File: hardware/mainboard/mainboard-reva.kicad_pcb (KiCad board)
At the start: 4 copper layers, 88 x 48 mm, 77 parts, among them J1 USB-C, J2 BATTERY, J3 SM05B-GHS-TB / ENCODER, J4 SM03B-GHS-TB / SNOOZE, J5 Molex 54550-2472 / GDEY037T03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, J6 Molex 54550-0672 / FL21 front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, J7 SPEAKER, J8 SM02B-GHS-TB / WAKE_LED, Q2 AO3400A / WAKE, U1 ESP32-S3-WROOM-1-N8, U2 BQ24074RGTR, U3 TPS62840DLCR, U4 RV-3028-C7, U5 VEML7700, U6 MAX98357AETE+T, U7 USBLC6-2SC6

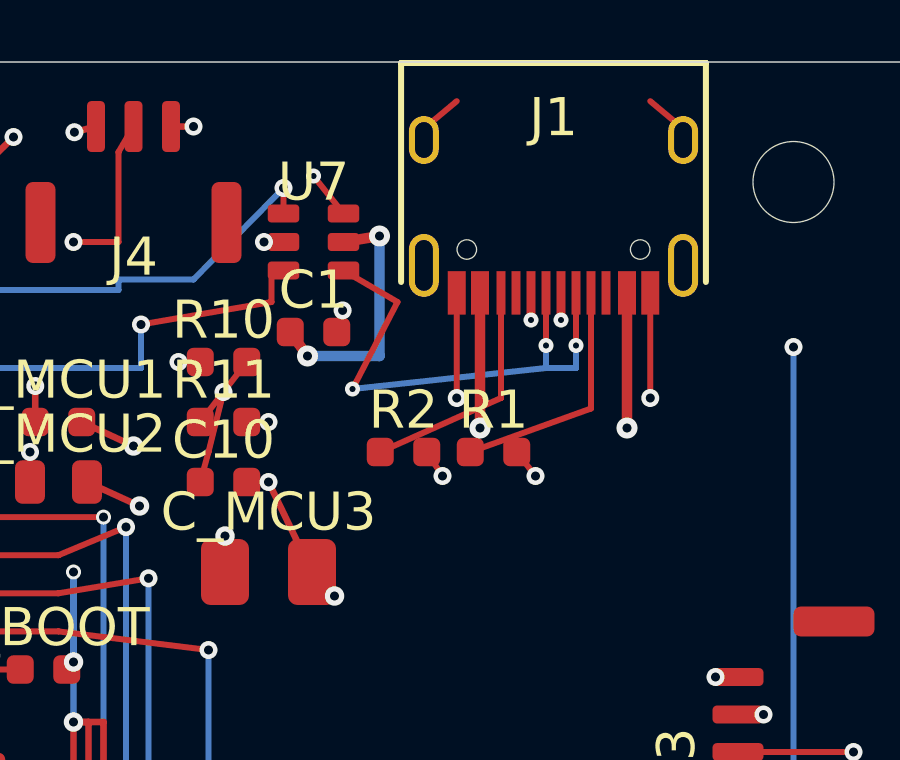
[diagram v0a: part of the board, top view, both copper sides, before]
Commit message: fix(mainboard): finish CC fanout and USB data clearances
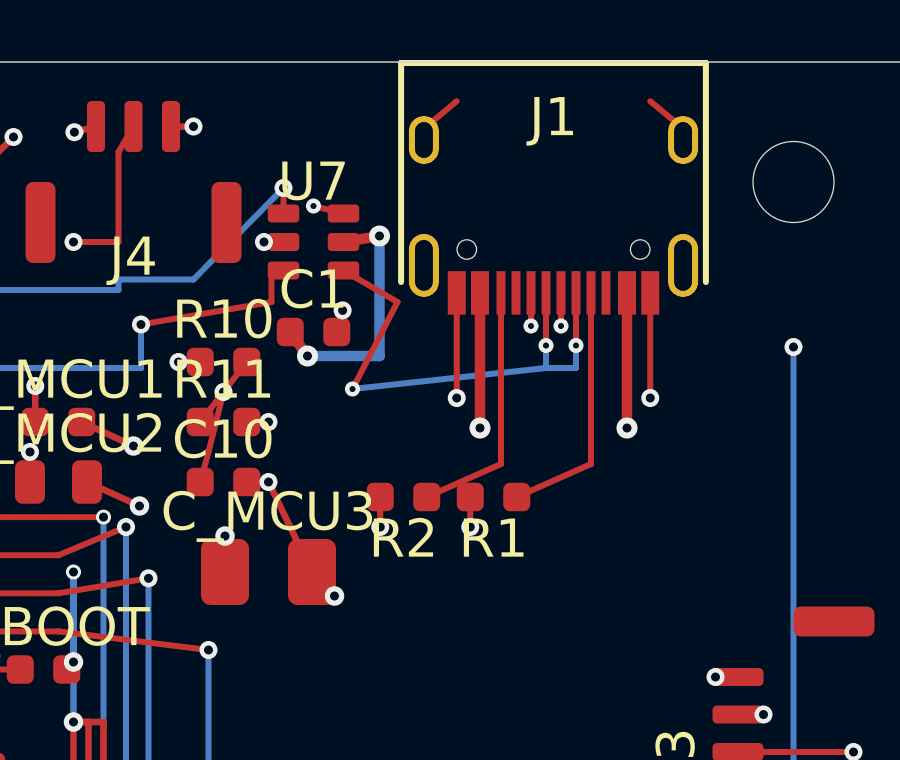
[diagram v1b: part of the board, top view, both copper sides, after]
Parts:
- moved R1 1.50 mm to (74.0, 14.5), turned to 180 degrees
- moved R2 1.50 mm to (71.0, 14.5), turned to 180 degrees
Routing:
- net USB_D+_CONN: track 18.1 -> 16.6 mm
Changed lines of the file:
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@@
     (pad "6" smd roundrect (at 1 -0.95) (size 1.05 0.6) (layers "F.Cu" "F.Paste" "F.Mask") (roundrect_rratio 0.2) (net 59 "USB_D+_CONN"))
   )
-  (footprint "Resistor_SMD:R_0603_1608Metric" (layer "F.Cu") (at 74.0 13.0)
+  (footprint "Resistor_SMD:R_0603_1608Metric" (layer "F.Cu") (at 74.0 14.5 180)
     (property "Reference" "R1" (at 0 -1.4) (layer "F.SilkS"))
     (property "Value" "5.1k CC1" (at 0 1.4) (layer "F.Fab") hide)
@@
     (pad "2" smd roundrect (at 0.775 0) (size 0.9 0.95) (layers "F.Cu" "F.Paste" "F.Mask") (roundrect_rratio 0.25) (net 1 "GND"))
   )
-  (footprint "Resistor_SMD:R_0603_1608Metric" (layer "F.Cu") (at 71.0 13.0)
+  (footprint "Resistor_SMD:R_0603_1608Metric" (layer "F.Cu") (at 71.0 14.5 180)
     (property "Reference" "R2" (at 0 -1.4) (layer "F.SilkS"))
     (property "Value" "5.1k CC2" (at 0 1.4) (layer "F.Fab") hide)
@@
   (segment (start 79.225 7.695) (end 79.225 11.20) (width 0.20) (layer "F.Cu") (net 1))
   (via (at 79.225 11.20) (size 0.60) (drill 0.30) (layers "F.Cu" "B.Cu") (net 1))
-  (segment (start 77.25 7.695) (end 77.25 11.55) (width 0.20) (layer "F.Cu") (net 21))
-  (segment (start 77.25 11.55) (end 73.225 13.00) (width 0.20) (layer "F.Cu") (net 21))
-  (segment (start 71.775 13.00) (end 72.30 13.80) (width 0.20) (layer "F.Cu") (net 1))
-  (via (at 72.30 13.80) (size 0.60) (drill 0.30) (layers "F.Cu" "B.Cu") (net 1))
-  (segment (start 74.25 7.695) (end 74.25 11.20) (width 0.20) (layer "F.Cu") (net 22))
-  (segment (start 74.25 11.20) (end 70.225 13.00) (width 0.20) (layer "F.Cu") (net 22))
-  (segment (start 74.775 13.00) (end 75.40 13.80) (width 0.20) (layer "F.Cu") (net 1))
-  (via (at 75.40 13.80) (size 0.60) (drill 0.30) (layers "F.Cu" "B.Cu") (net 1))
-  (segment (start 75.25 7.695) (end 75.25 8.60) (width 0.20) (layer "F.Cu") (net 59))
-  (via (at 75.25 8.60) (size 0.50) (drill 0.20) (layers "F.Cu" "B.Cu") (net 59))
-  (segment (start 76.25 7.695) (end 76.25 8.60) (width 0.20) (layer "F.Cu") (net 59))
-  (via (at 76.25 8.60) (size 0.50) (drill 0.20) (layers "F.Cu" "B.Cu") (net 59))
-  (segment (start 75.25 8.60) (end 75.25 9.80) (width 0.20) (layer "In1.Cu") (net 59))
-  (segment (start 76.25 8.60) (end 76.25 9.80) (width 0.20) (layer "In1.Cu") (net 59))
+  (segment (start 77.25 7.695) (end 77.25 13.40) (width 0.20) (layer "F.Cu") (net 21))
+  (segment (start 77.25 13.40) (end 74.775 14.50) (width 0.20) (layer "F.Cu") (net 21))
+  (segment (start 73.225 14.50) (end 73.225 15.50) (width 0.20) (layer "F.Cu") (net 1))
+  (via (at 73.225 15.50) (size 0.60) (drill 0.30) (layers "F.Cu" "B.Cu") (net 1))
+  (segment (start 74.25 7.695) (end 74.25 13.40) (width 0.20) (layer "F.Cu") (net 22))
+  (segment (start 74.25 13.40) (end 71.775 14.50) (width 0.20) (layer "F.Cu") (net 22))
+  (segment (start 70.225 14.50) (end 70.225 15.50) (width 0.20) (layer "F.Cu") (net 1))
+  (via (at 70.225 15.50) (size 0.60) (drill 0.30) (layers "F.Cu" "B.Cu") (net 1))
+  (segment (start 75.25 7.695) (end 75.25 8.80) (width 0.20) (layer "F.Cu") (net 59))
+  (via (at 75.25 8.80) (size 0.50) (drill 0.20) (layers "F.Cu" "B.Cu") (net 59))
+  (segment (start 76.25 7.695) (end 76.25 8.80) (width 0.20) (layer "F.Cu") (net 59))
+  (via (at 76.25 8.80) (size 0.50) (drill 0.20) (layers "F.Cu" "B.Cu") (net 59))
+  (segment (start 75.25 8.80) (end 75.25 9.80) (width 0.20) (layer "In1.Cu") (net 59))
+  (segment (start 76.25 8.80) (end 76.25 9.80) (width 0.20) (layer "In1.Cu") (net 59))
   (segment (start 76.25 9.80) (end 75.25 9.80) (width 0.20) (layer "In1.Cu") (net 59))
   (segment (start 75.25 9.80) (end 72.00 10.20) (width 0.20) (layer "In1.Cu") (net 59))
   (segment (start 72.00 10.20) (end 68.00 6.20) (width 0.20) (layer "In1.Cu") (net 59))
-  (segment (start 68.00 6.20) (end 68.00 3.80) (width 0.20) (layer "In1.Cu") (net 59))
-  (via (at 68.00 3.80) (size 0.50) (drill 0.20) (layers "F.Cu" "B.Cu") (net 59))
-  (segment (start 68.00 3.80) (end 69.0 5.05) (width 0.20) (layer "F.Cu") (net 59))
+  (segment (start 68.00 6.20) (end 68.00 4.80) (width 0.20) (layer "In1.Cu") (net 59))
+  (via (at 68.00 4.80) (size 0.50) (drill 0.20) (layers "F.Cu" "B.Cu") (net 59))
+  (segment (start 68.00 4.80) (end 69.0 5.05) (width 0.20) (layer "F.Cu") (net 59))
   (segment (start 75.75 7.695) (end 75.75 9.45) (width 0.20) (layer "F.Cu") (net 60))
   (via (at 75.75 9.45) (size 0.50) (drill 0.20) (layers "F.Cu" "B.Cu") (net 60))

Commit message: fix(mainboard): clear final USB CC and differential breakout conflicts
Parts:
- moved R1 6.00 mm to (80.0, 14.5)
- moved R2 1.00 mm to (72.0, 14.5)
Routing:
- net GND: track 109.5 -> 112.5 mm
- net USB_D+_CONN: track 16.6 -> 17.9 mm
- net USB_CC1: track 8.41 -> 9.40 mm
- net USB_CC2: track 8.41 -> 7.55 mm
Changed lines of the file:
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@@
     (pad "6" smd roundrect (at 1 -0.95) (size 1.05 0.6) (layers "F.Cu" "F.Paste" "F.Mask") (roundrect_rratio 0.2) (net 59 "USB_D+_CONN"))
   )
-  (footprint "Resistor_SMD:R_0603_1608Metric" (layer "F.Cu") (at 74.0 14.5 180)
+  (footprint "Resistor_SMD:R_0603_1608Metric" (layer "F.Cu") (at 80.0 14.5 180)
     (property "Reference" "R1" (at 0 -1.4) (layer "F.SilkS"))
     (property "Value" "5.1k CC1" (at 0 1.4) (layer "F.Fab") hide)
@@
     (pad "2" smd roundrect (at 0.775 0) (size 0.9 0.95) (layers "F.Cu" "F.Paste" "F.Mask") (roundrect_rratio 0.25) (net 1 "GND"))
   )
-  (footprint "Resistor_SMD:R_0603_1608Metric" (layer "F.Cu") (at 71.0 14.5 180)
+  (footprint "Resistor_SMD:R_0603_1608Metric" (layer "F.Cu") (at 72.0 14.5 180)
     (property "Reference" "R2" (at 0 -1.4) (layer "F.SilkS"))
     (property "Value" "5.1k CC2" (at 0 1.4) (layer "F.Fab") hide)
@@
   (via (at 79.225 11.20) (size 0.60) (drill 0.30) (layers "F.Cu" "B.Cu") (net 1))
   (segment (start 77.25 7.695) (end 77.25 13.40) (width 0.20) (layer "F.Cu") (net 21))
-  (segment (start 77.25 13.40) (end 74.775 14.50) (width 0.20) (layer "F.Cu") (net 21))
-  (segment (start 73.225 14.50) (end 73.225 15.50) (width 0.20) (layer "F.Cu") (net 1))
-  (via (at 73.225 15.50) (size 0.60) (drill 0.30) (layers "F.Cu" "B.Cu") (net 1))
+  (segment (start 77.25 13.40) (end 80.775 14.50) (width 0.20) (layer "F.Cu") (net 21))
+  (segment (start 79.225 14.50) (end 79.225 17.00) (width 0.20) (layer "F.Cu") (net 1))
+  (via (at 79.225 17.00) (size 0.60) (drill 0.30) (layers "F.Cu" "B.Cu") (net 1))
   (segment (start 74.25 7.695) (end 74.25 13.40) (width 0.20) (layer "F.Cu") (net 22))
-  (segment (start 74.25 13.40) (end 71.775 14.50) (width 0.20) (layer "F.Cu") (net 22))
-  (segment (start 70.225 14.50) (end 70.225 15.50) (width 0.20) (layer "F.Cu") (net 1))
-  (via (at 70.225 15.50) (size 0.60) (drill 0.30) (layers "F.Cu" "B.Cu") (net 1))
+  (segment (start 74.25 13.40) (end 72.775 14.50) (width 0.20) (layer "F.Cu") (net 22))
+  (segment (start 71.225 14.50) (end 71.225 17.00) (width 0.20) (layer "F.Cu") (net 1))
+  (via (at 71.225 17.00) (size 0.60) (drill 0.30) (layers "F.Cu" "B.Cu") (net 1))
   (segment (start 75.25 7.695) (end 75.25 8.80) (width 0.20) (layer "F.Cu") (net 59))
   (via (at 75.25 8.80) (size 0.50) (drill 0.20) (layers "F.Cu" "B.Cu") (net 59))
   (segment (start 76.25 7.695) (end 76.25 8.80) (width 0.20) (layer "F.Cu") (net 59))
   (via (at 76.25 8.80) (size 0.50) (drill 0.20) (layers "F.Cu" "B.Cu") (net 59))
-  (segment (start 75.25 8.80) (end 75.25 9.80) (width 0.20) (layer "In1.Cu") (net 59))
-  (segment (start 76.25 8.80) (end 76.25 9.80) (width 0.20) (layer "In1.Cu") (net 59))
-  (segment (start 76.25 9.80) (end 75.25 9.80) (width 0.20) (layer "In1.Cu") (net 59))
-  (segment (start 75.25 9.80) (end 72.00 10.20) (width 0.20) (layer "In1.Cu") (net 59))
-  (segment (start 72.00 10.20) (end 68.00 6.20) (width 0.20) (layer "In1.Cu") (net 59))
+  (segment (start 75.25 8.80) (end 75.25 10.30) (width 0.20) (layer "In1.Cu") (net 59))
+  (segment (start 76.25 8.80) (end 76.25 10.30) (width 0.20) (layer "In1.Cu") (net 59))
+  (segment (start 76.25 10.30) (end 75.25 10.30) (width 0.20) (layer "In1.Cu") (net 59))
+  (segment (start 75.25 10.30) (end 72.00 10.70) (width 0.20) (layer "In1.Cu") (net 59))
+  (segment (start 72.00 10.70) (end 68.00 6.20) (width 0.20) (layer "In1.Cu") (net 59))
   (segment (start 68.00 6.20) (end 68.00 4.80) (width 0.20) (layer "In1.Cu") (net 59))
   (via (at 68.00 4.80) (size 0.50) (drill 0.20) (layers "F.Cu" "B.Cu") (net 59))

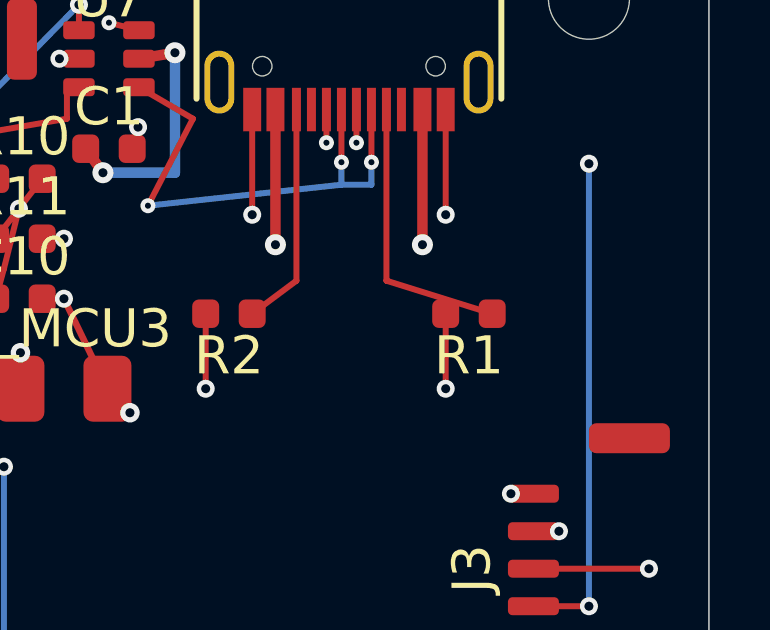
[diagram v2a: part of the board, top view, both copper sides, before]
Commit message: fix(mainboard): orient CC1 pulldown for clean fanout
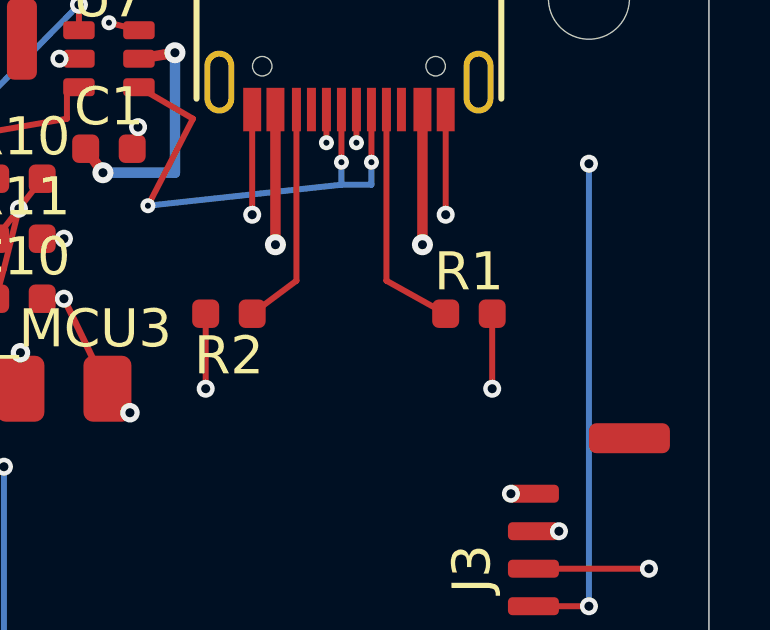
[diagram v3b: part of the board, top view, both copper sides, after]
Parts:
- turned R1 to 0 degrees
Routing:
- net USB_CC1: track 9.40 -> 7.97 mm
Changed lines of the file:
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@@
     (pad "6" smd roundrect (at 1 -0.95) (size 1.05 0.6) (layers "F.Cu" "F.Paste" "F.Mask") (roundrect_rratio 0.2) (net 59 "USB_D+_CONN"))
   )
-  (footprint "Resistor_SMD:R_0603_1608Metric" (layer "F.Cu") (at 80.0 14.5 180)
+  (footprint "Resistor_SMD:R_0603_1608Metric" (layer "F.Cu") (at 80.0 14.5)
     (property "Reference" "R1" (at 0 -1.4) (layer "F.SilkS"))
     (property "Value" "5.1k CC1" (at 0 1.4) (layer "F.Fab") hide)
@@
   (via (at 79.225 11.20) (size 0.60) (drill 0.30) (layers "F.Cu" "B.Cu") (net 1))
   (segment (start 77.25 7.695) (end 77.25 13.40) (width 0.20) (layer "F.Cu") (net 21))
-  (segment (start 77.25 13.40) (end 80.775 14.50) (width 0.20) (layer "F.Cu") (net 21))
-  (segment (start 79.225 14.50) (end 79.225 17.00) (width 0.20) (layer "F.Cu") (net 1))
-  (via (at 79.225 17.00) (size 0.60) (drill 0.30) (layers "F.Cu" "B.Cu") (net 1))
+  (segment (start 77.25 13.40) (end 79.225 14.50) (width 0.20) (layer "F.Cu") (net 21))
+  (segment (start 80.775 14.50) (end 80.775 17.00) (width 0.20) (layer "F.Cu") (net 1))
+  (via (at 80.775 17.00) (size 0.60) (drill 0.30) (layers "F.Cu" "B.Cu") (net 1))
   (segment (start 74.25 7.695) (end 74.25 13.40) (width 0.20) (layer "F.Cu") (net 22))
   (segment (start 74.25 13.40) (end 72.775 14.50) (width 0.20) (layer "F.Cu") (net 22))

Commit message: fix(mainboard): match EPD inductor land pattern to locked Wurth part
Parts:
- removed the L_EPD at (30.0, 35.0)
- added L_EPD: 74438335100 10uH, ENKU_Clock:WE-MAPI_3015_74438335100, F.Cu at (30.0, 35.0)
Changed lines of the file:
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@@
     (pad "2" smd roundrect (at 0.95 0) (size 1 1.45) (layers "F.Cu" "F.Paste" "F.Mask") (roundrect_rratio 0.25) (net 1 "GND"))
   )
-  (footprint "Inductor_SMD:L_3.0x3.0mm_H1.5mm" (layer "F.Cu") (at 30 35)
+  (footprint "ENKU_Clock:WE-MAPI_3015_74438335100" (layer "F.Cu") (at 30 35)
     (property "Reference" "L_EPD" (at 0 -2.2) (layer "F.SilkS"))
-    (property "Value" "10uH >=1A" (at 0 2.2) (layer "F.Fab") hide)
-    (pad "1" smd rect (at -1.2 0) (size 1.2 2.4) (layers "F.Cu" "F.Paste" "F.Mask") (net 6 "+3V3"))
-    (pad "2" smd rect (at 1.2 0) (size 1.2 2.4) (layers "F.Cu" "F.Paste" "F.Mask") (net 54 "EPD_SW"))
+    (property "Value" "74438335100 10uH" (at 0 2.2) (layer "F.Fab") hide)
+    (attr smd)
+    (fp_rect (start -1.5 -1.5) (end 1.5 1.5) (stroke (width 0.1) (type default)) (fill none) (layer "F.Fab"))
+    (fp_rect (start -1.7 -1.7) (end 1.7 1.7) (stroke (width 0.05) (type default)) (fill none) (layer "F.CrtYd"))
+    (pad "1" smd rect (at -1.05 0) (size 1.3 3.4) (layers "F.Cu" "F.Paste" "F.Mask") (net 6 "+3V3"))
+    (pad "2" smd rect (at 1.05 0) (size 1.3 3.4) (layers "F.Cu" "F.Paste" "F.Mask") (net 54 "EPD_SW"))
   )
   (footprint "Package_TO_SOT_SMD:SOT-323_SC-70" (layer "F.Cu") (at 34.5 35)
